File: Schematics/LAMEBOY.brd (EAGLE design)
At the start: 45.7 x 67.3 mm, 65 parts, among them IC1 PCF8574T, IC3 MCP73831, Q1 12MHz, U1 USD-SOCKETMICROSDEBAY, U2 USB

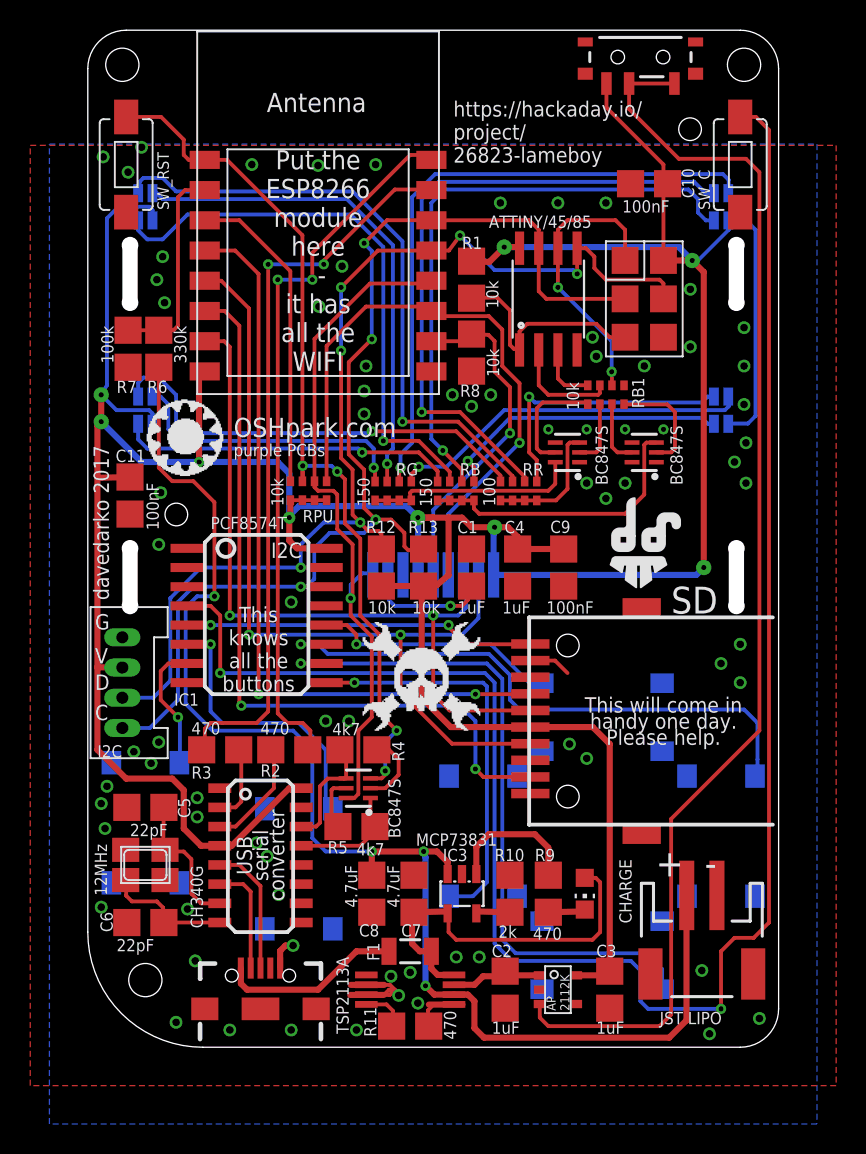
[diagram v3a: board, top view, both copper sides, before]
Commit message: moved sd slot slightley
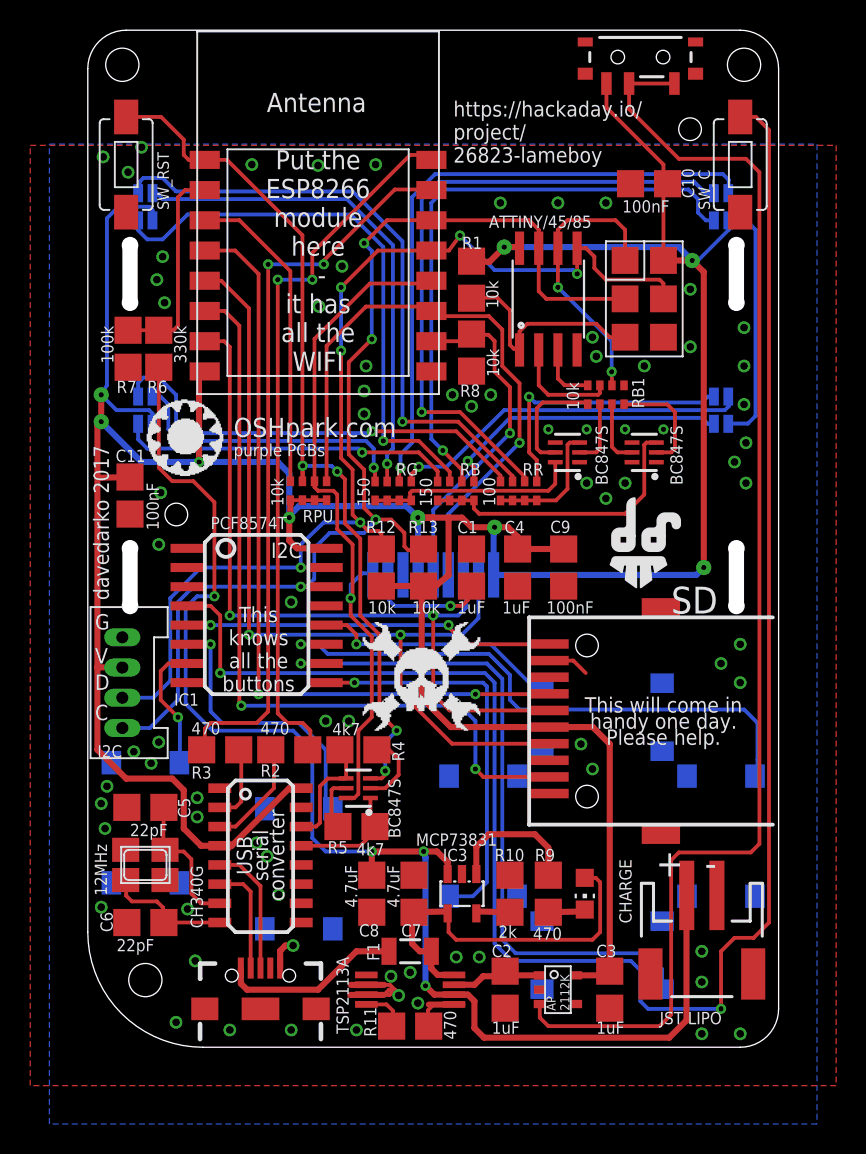
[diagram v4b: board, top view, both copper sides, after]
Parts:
- moved U1 1.27 mm to (35.6, 21.6)
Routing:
- net VREG_EN: track 83.4 -> 86.1 mm
- net ESP_SCKL: track 57.6 -> 58.9 mm
- net ESP_MOSI: track 49.8 -> 51.1 mm
- net ESP_MISO: track 50.8 -> 52.1 mm
- net SD_IN: track 23.3 -> 24.6 mm
- net SD_CS: track 50.0 -> 51.3 mm
- net GND: track 17.8 -> 17.7 mm, vias 76 -> 77
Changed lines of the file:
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@@
 <setting verticaltext="up"/>
 </settings>
-<grid distance="0.05" unitdist="inch" unit="inch" style="lines" multiple="1" display="yes" altdistance="0.0025" altunitdist="inch" altunit="inch"/>
+<grid distance="0.05" unitdist="inch" unit="inch" style="lines" multiple="1" display="yes" altdistance="0.01" altunitdist="inch" altunit="inch"/>
 <layers>
 <layer number="1" name="Top" color="4" fill="1" visible="yes" active="yes"/>
@@
 <attribute name="VALUE" x="45.88" y="55.42" size="0.762" layer="27" rot="R90"/>
 </element>
-<element name="U1" library="SparkFun-Connectors" package="MICRO-SD-SOCKET-EBAY" value="USD-SOCKETMICROSDEBAY" x="34.29" y="21.59" rot="R270"/>
+<element name="U1" library="SparkFun-Connectors" package="MICRO-SD-SOCKET-EBAY" value="USD-SOCKETMICROSDEBAY" x="35.56" y="21.59" rot="R270"/>
 <element name="U2" library="SparkFun-Connectors" package="USB-AB-MICRO-SMD_V03" value="USB" x="11.43" y="2.54" smashed="yes" rot="R90">
 <attribute name="PROD_ID" value="CONN-11794" x="11.43" y="2.54" size="1.778" layer="27" rot="R90" display="off"/>
@@
 <contactref element="U$4" pad="2"/>
 <contactref element="U$4" pad="3"/>
-<via x="41.148" y="0.889" extent="1-16" drill="0.5"/>
-<via x="40.64" y="5.08" extent="1-16" drill="0.5"/>
-<via x="44.45" y="1.905" extent="1-16" drill="0.5"/>
+<via x="40.64" y="0.889" extent="1-16" drill="0.5"/>
+<via x="40.64" y="4.318" extent="1-16" drill="0.5"/>
+<via x="43.18" y="0.889" extent="1-16" drill="0.5"/>
 <contactref element="U$6" pad="4"/>
 <contactref element="U$7" pad="4"/>
@@
 <contactref element="C10" pad="P$1"/>
 <contactref element="C11" pad="P$1"/>
-<wire x1="29.29" y1="25.59" x2="30.925" y2="25.59" width="0.254" layer="1"/>
-<wire x1="30.925" y1="25.59" x2="31.75" y2="24.765" width="0.254" layer="1"/>
-<via x="31.877" y="20.066" extent="1-16" drill="0.5"/>
-<via x="33.02" y="19.1135" extent="1-16" drill="0.5"/>
+<wire x1="30.56" y1="25.59" x2="32.1315" y2="25.59" width="0.254" layer="1"/>
+<wire x1="32.1315" y1="25.59" x2="32.9565" y2="24.765" width="0.254" layer="1"/>
+<via x="32.639" y="20.066" extent="1-16" drill="0.5"/>
+<via x="33.401" y="18.415" extent="1-16" drill="0.5"/>
 <via x="18.288" y="43.434" extent="1-16" drill="0.5"/>
 <via x="26.67" y="43.18" extent="1-16" drill="0.5"/>
@@
 <via x="5.08" y="49.276" extent="1-16" drill="0.5"/>
 <via x="11.176" y="13.5255" extent="1-16" drill="0.5"/>
+<via x="40.64" y="6.35" extent="1-16" drill="0.5"/>
 </signal>
 <signal name="VCC">
@@
 <wire x1="2.286" y1="25.13" x2="2.27" y2="25.146" width="0.4064" layer="1"/>
 <wire x1="2.27" y1="25.146" x2="0.635" y2="25.146" width="0.4064" layer="1"/>
-<wire x1="29.29" y1="21.19" x2="33.42" y2="21.19" width="0.4064" layer="1"/>
+<wire x1="30.56" y1="21.19" x2="33.42" y2="21.19" width="0.4064" layer="1"/>
 <wire x1="33.42" y1="21.19" x2="34.544" y2="20.066" width="0.4064" layer="1"/>
 <wire x1="34.544" y1="20.066" x2="34.544" y2="5.035" width="0.4064" layer="1"/>
@@
 <wire x1="22.87691875" y1="35.052" x2="21.86091875" y2="35.03508125" width="0.4064" layer="1"/>
 <wire x1="21.86091875" y1="35.03508125" x2="21.844" y2="35.052" width="0.254" layer="1"/>
-<wire x1="29.29" y1="21.19" x2="24.022" y2="21.19" width="0.4064" layer="1"/>
+<wire x1="30.56" y1="21.19" x2="24.022" y2="21.19" width="0.4064" layer="1"/>
 <wire x1="24.022" y1="21.19" x2="22.098" y2="23.114" width="0.4064" layer="1"/>
 <wire x1="22.098" y1="23.114" x2="22.098" y2="29.972" width="0.4064" layer="1"/>
@@
 <wire x1="24.892" y1="31.22811875" x2="24.86091875" y2="31.2592" width="0.254" layer="16"/>
 <contactref element="U1" pad="P$3"/>
-<wire x1="29.29" y1="22.29" x2="23.938" y2="22.29" width="0.254" layer="1"/>
+<wire x1="30.56" y1="22.29" x2="23.938" y2="22.29" width="0.254" layer="1"/>
 <wire x1="23.938" y1="22.29" x2="22.86" y2="23.368" width="0.254" layer="1"/>
 <wire x1="22.86" y1="23.368" x2="22.86" y2="28.575" width="0.254" layer="1"/>
@@
 <via x="20.701" y="27.305" extent="1-16" drill="0.3302"/>
 <wire x1="24.106" y1="20.09" x2="20.701" y2="23.495" width="0.254" layer="1"/>
-<wire x1="29.29" y1="20.09" x2="24.106" y2="20.09" width="0.254" layer="1"/>
+<wire x1="30.56" y1="20.09" x2="24.106" y2="20.09" width="0.254" layer="1"/>
 </signal>
 <signal name="BLUE_LED">
@@
 <wire x1="25.654" y1="21.59" x2="25.654" y2="18.415" width="0.254" layer="16"/>
 <via x="25.654" y="18.415" extent="1-16" drill="0.3302"/>
-<wire x1="29.29" y1="17.89" x2="26.179" y2="17.89" width="0.254" layer="1"/>
+<wire x1="30.56" y1="17.89" x2="26.179" y2="17.89" width="0.254" layer="1"/>
 <wire x1="26.179" y1="17.89" x2="25.654" y2="18.415" width="0.254" layer="1"/>
 </signal>
@@
 <wire x1="30.48" y1="1.397" x2="37.846" y2="1.397" width="0.254" layer="1"/>
 <wire x1="37.846" y1="1.397" x2="38.608" y2="2.159" width="0.254" layer="1"/>
-<wire x1="38.608" y1="2.159" x2="38.608" y2="15.113" width="0.254" layer="1"/>
-<wire x1="38.608" y1="15.113" x2="44.45" y2="20.955" width="0.254" layer="1"/>
-<wire x1="44.45" y1="20.955" x2="44.45" y2="57.912" width="0.254" layer="1"/>
+<wire x1="38.608" y1="2.159" x2="38.608" y2="12.3825" width="0.254" layer="1"/>
+<wire x1="38.608" y1="12.3825" x2="39.116" y2="12.8905" width="0.254" layer="1"/>
+<wire x1="39.116" y1="12.8905" x2="43.8785" y2="12.8905" width="0.254" layer="1"/>
+<wire x1="43.8785" y1="12.8905" x2="44.45" y2="13.462" width="0.254" layer="1"/>
+<wire x1="44.45" y1="13.462" x2="44.45" y2="57.912" width="0.254" layer="1"/>
 <wire x1="44.45" y1="57.912" x2="43.561" y2="58.801" width="0.254" layer="1"/>
 <wire x1="43.561" y1="58.801" x2="39.116" y2="58.801" width="0.254" layer="1"/>
@@
 <via x="25.654" y="23.368" extent="1-16" drill="0.3302"/>
 <wire x1="25.654" y1="23.368" x2="29.268" y2="23.368" width="0.254" layer="1"/>
-<wire x1="29.268" y1="23.368" x2="29.29" y2="23.39" width="0.254" layer="1"/>
+<wire x1="29.268" y1="23.368" x2="30.56" y2="23.39" width="0.254" layer="1"/>
 </signal>
 <signal name="SD_IN">
@@
 <wire x1="23.876" y1="27.813" x2="25.019" y2="26.67" width="0.254" layer="1"/>
 <wire x1="25.019" y1="26.67" x2="29.27" y2="26.67" width="0.254" layer="1"/>
-<wire x1="29.27" y1="26.67" x2="29.29" y2="26.69" width="0.254" layer="1"/>
+<wire x1="29.27" y1="26.67" x2="30.56" y2="26.69" width="0.254" layer="1"/>
 </signal>
 </signals>
